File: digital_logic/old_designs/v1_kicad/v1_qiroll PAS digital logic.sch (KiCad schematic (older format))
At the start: 43 parts, among them J1 led_sw1, J2 mode_thr_batt, J3 pas_sense, J4 brk_sense, J5 jumper, U1 14538, U2 4023, U3 4027, U4 14538, U5 L7805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

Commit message: pcb revision, add circuit sim, old kicad files to reference for v1 board repairs
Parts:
- removed D1: Reverse Protect Diode, Diode_SMD:D_MiniMELF, symbol Device:D
- removed F1: PTC, Fuse:Fuse_1206_3216Metric, symbol Device:Polyfuse_Small
- removed R11: 10k, Resistor_SMD:R_0603_1608Metric, symbol Device:R
- C11: value .1u -> 1u
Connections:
- wire segments 115 -> 106
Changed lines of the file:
@@
 $EndComp
 Wire Wire Line
-	8700 1750 8750 1750
+	8700 1750 8900 1750
 $Comp
 L power:GND #PWR0144
@@
 Wire Wire Line
 	7150 1550 7150 1500
+Wire Wire Line
+	7850 1750 8000 1750
 $Comp
 L power:PWR_FLAG #FLG0101
@@
 	0    -1   -1   0
 $EndComp
+Wire Wire Line
+	6150 2200 6150 2100
 $Comp
 L Device:R R9
@@
 U 1 1 60E015DA
 P 6200 2300
-F 0 "C11" V 5950 2350 50  0000 C CNN
-F 1 ".1u" V 6050 2350 50  0000 C CNN
+F 0 "C11" V 5948 2300 50  0000 C CNN
+F 1 "1u" V 6039 2300 50  0000 C CNN
 F 2 "Capacitor_SMD:C_0603_1608Metric" H 6238 2150 50  0001 C CNN
 F 3 "https://www.digikey.com/en/products/detail/tdk-corporation/C1608X7R1C105K080AC/634399" H 6200 2300 50  0001 C CNN
@@
 	-1   0    0    1
 $EndComp
-Text GLabel 7050 1050 3    50   Input ~ 0
+Text GLabel 7050 900  3    50   Input ~ 0
 BRK
 Text GLabel 5950 3400 0    50   Input ~ 0
@@
 	6250 1650 6250 1500
 Wire Wire Line
+	6150 1750 6700 1750
+Wire Wire Line
 	5900 2300 5950 2300
 Wire Wire Line
@@
 	5950 2300 6050 2300
 Connection ~ 5950 2300
+Wire Wire Line
+	6150 2200 6900 2200
 Wire Wire Line
 	6900 3400 6600 3400
@@
 Wire Wire Line
 	6600 2850 6900 2850
+Wire Wire Line
+	6900 2200 6900 2850
+Connection ~ 6900 2850
 Wire Wire Line
 	6900 2850 6900 3400
@@
 Wire Wire Line
 	7700 1750 7850 1750
+Wire Wire Line
+	7400 1750 6700 1750
+Connection ~ 6700 1750
 $Comp
 L 4xxx:14538 U1
@@
 	0    1    1    0
 $EndComp
-Wire Wire Line
-	7050 1050 7050 1000
-Wire Wire Line
-	7050 1000 7250 1000
-Connection ~ 7050 1000
-Wire Wire Line
-	7050 1000 7050 900
-$Comp
-L Device:R R11
-U 1 1 60E0D46A
-P 7400 1000
-F 0 "R11" V 7200 1000 50  0000 C CNN
-F 1 "10k" V 7300 1000 50  0000 C CNN
-F 2 "Resistor_SMD:R_0603_1608Metric" V 7330 1000 50  0001 C CNN
-F 3 "~" H 7400 1000 50  0001 C CNN
-	1    7400 1000
-	0    -1   -1   0
-$EndComp
-$Comp
-L power:GND #PWR0165
-U 1 1 60E123A7
-P 7550 1000
-F 0 "#PWR0165" H 7550 750 50  0001 C CNN
-F 1 "GND" V 7555 872 50  0000 R CNN
-F 2 "" H 7550 1000 50  0001 C CNN
-F 3 "" H 7550 1000 50  0001 C CNN
-	1    7550 1000
-	0    -1   -1   0
-$EndComp
-$Comp
-L Device:Polyfuse_Small F1
-U 1 1 60E03DF4
-P 6700 1850
-F 0 "F1" V 6495 1850 50  0000 C CNN
-F 1 "PTC" V 6586 1850 50  0000 C CNN
-F 2 "Fuse:Fuse_1206_3216Metric" H 6750 1650 50  0001 L CNN
-F 3 "https://www.digikey.com/en/products/detail/bel-fuse-inc/0ZCJ0012FF2E/4156129~" H 6700 1850 50  0001 C CNN
-	1    6700 1850
-	0    1    1    0
-$EndComp
-Wire Wire Line
-	7150 1750 7400 1750
-Wire Wire Line
-	7150 1750 7150 1850
-Wire Wire Line
-	7150 1850 6800 1850
-Wire Wire Line
-	6600 1850 6450 1850
-Wire Wire Line
-	6450 1850 6450 1750
-Wire Wire Line
-	6450 1750 6150 1750
-$Comp
-L Device:D D1
-U 1 1 60E52D25
-P 8400 1350
-F 0 "D1" H 8400 1567 50  0000 C CNN
-F 1 "Reverse Protect Diode" H 8400 1476 50  0000 C CNN
-F 2 "Diode_SMD:D_MiniMELF" H 8400 1350 50  0001 C CNN
-F 3 "https://www.digikey.com/en/products/detail/vishay-general-semiconductor-diodes-division/LL4150GS18/4810537" H 8400 1350 50  0001 C CNN
-	1    8400 1350
-	1    0    0    -1
-$EndComp
-Wire Wire Line
-	8550 1350 8750 1350
-Wire Wire Line
-	8750 1350 8750 1750
-Connection ~ 8750 1750
-Wire Wire Line
-	8750 1750 8900 1750
-Wire Wire Line
-	7850 1750 8100 1750
-Wire Wire Line
-	7400 1350 7400 1750
-Wire Wire Line
-	7400 1350 8250 1350
-Connection ~ 7400 1750
-Wire Wire Line
-	6150 2100 6600 2100
-$Comp
-L power:VDD #PWR?
-U 1 1 60F0AE87
-P 6600 2100
-F 0 "#PWR?" H 6600 1950 50  0001 C CNN
-F 1 "VDD" V 6615 2228 50  0000 L CNN
-F 2 "" H 6600 2100 50  0001 C CNN
-F 3 "" H 6600 2100 50  0001 C CNN
-	1    6600 2100
-	0    1    1    0
-$EndComp
+Connection ~ 8000 1750
+Wire Wire Line
+	8000 1750 8100 1750
 $EndSCHEMATC

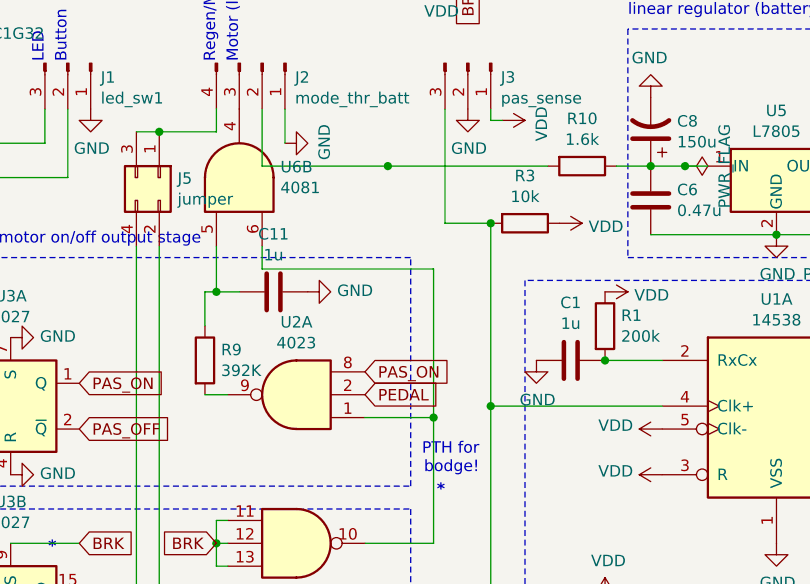
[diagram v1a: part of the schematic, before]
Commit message: add old design safety notes, delete faulty gerbers
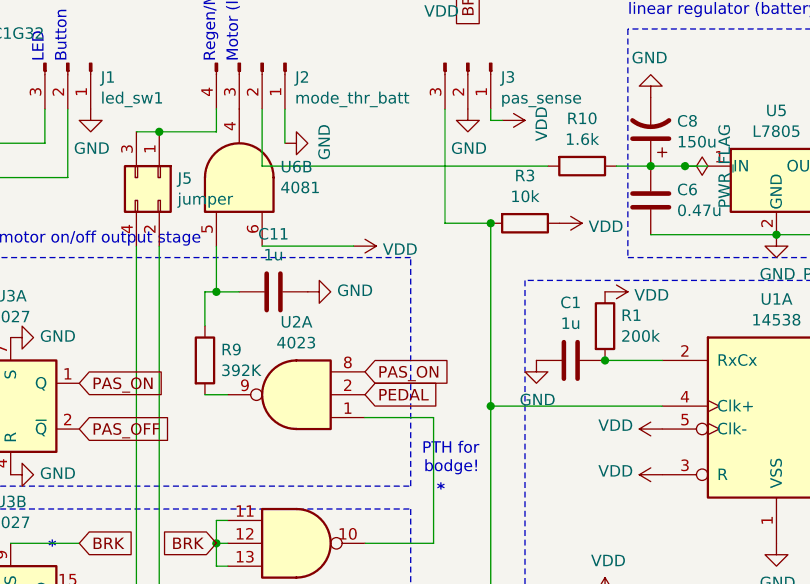
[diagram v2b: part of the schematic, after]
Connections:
- net VCC: now also U6.6
- net at U2.1, U2.10: no longer U6.6
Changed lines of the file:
@@
 	0    -1   -1   0
 $EndComp
-Wire Wire Line
-	6150 2200 6150 2100
 $Comp
 L Device:R R9
@@
 	6250 1650 6250 1500
 Wire Wire Line
-	6150 1750 6700 1750
-Wire Wire Line
 	5900 2300 5950 2300
 Wire Wire Line
@@
 	5950 2300 6050 2300
 Connection ~ 5950 2300
-Wire Wire Line
-	6150 2200 6900 2200
 Wire Wire Line
 	6900 3400 6600 3400
@@
 Wire Wire Line
 	6600 2850 6900 2850
-Wire Wire Line
-	6900 2200 6900 2850
-Connection ~ 6900 2850
 Wire Wire Line
 	6900 2850 6900 3400
@@
 Wire Wire Line
 	7700 1750 7850 1750
-Wire Wire Line
-	7400 1750 6700 1750
-Connection ~ 6700 1750
 $Comp
 L 4xxx:14538 U1
@@
 Wire Wire Line
 	8000 1750 8100 1750
+Wire Wire Line
+	6150 1750 7400 1750
+Wire Wire Line
+	6150 2100 6550 2100
+$Comp
+L power:VDD #PWR?
+U 1 1 60F494E6
+P 6550 2100
+F 0 "#PWR?" H 6550 1950 50  0001 C CNN
+F 1 "VDD" V 6565 2228 50  0000 L CNN
+F 2 "" H 6550 2100 50  0001 C CNN
+F 3 "" H 6550 2100 50  0001 C CNN
+	1    6550 2100
+	0    1    1    0
+$EndComp
 $EndSCHEMATC
